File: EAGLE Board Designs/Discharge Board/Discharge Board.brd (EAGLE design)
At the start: 57.1 x 77.1 mm, 21 parts, among them J100 CONNECTOR-2_MICROFIT_SMD_RIGH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, J101 CONNECTOR-2_MICROFIT_SMD_RIGH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, K1 RELAY_SPST_NC_POLARIZED_D_24

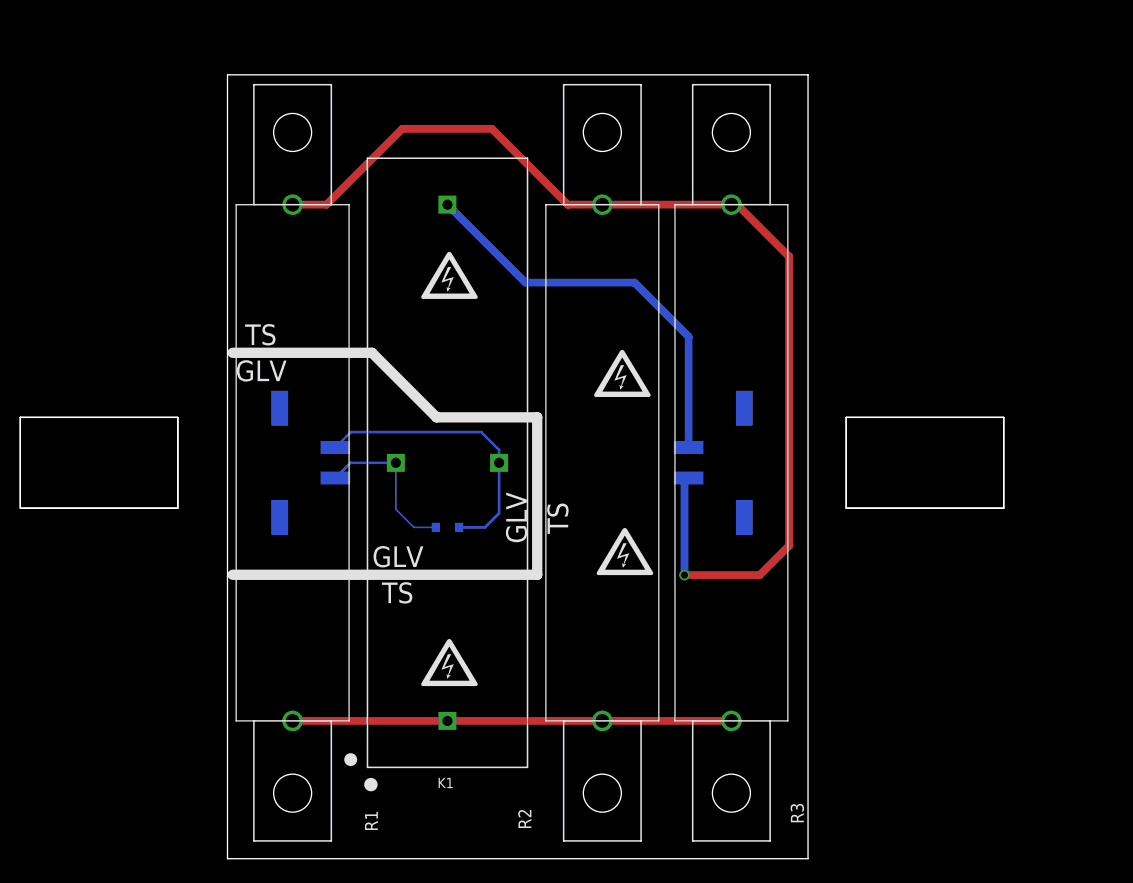
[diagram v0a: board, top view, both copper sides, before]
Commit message: Replace B20 with B20-SHORTENED
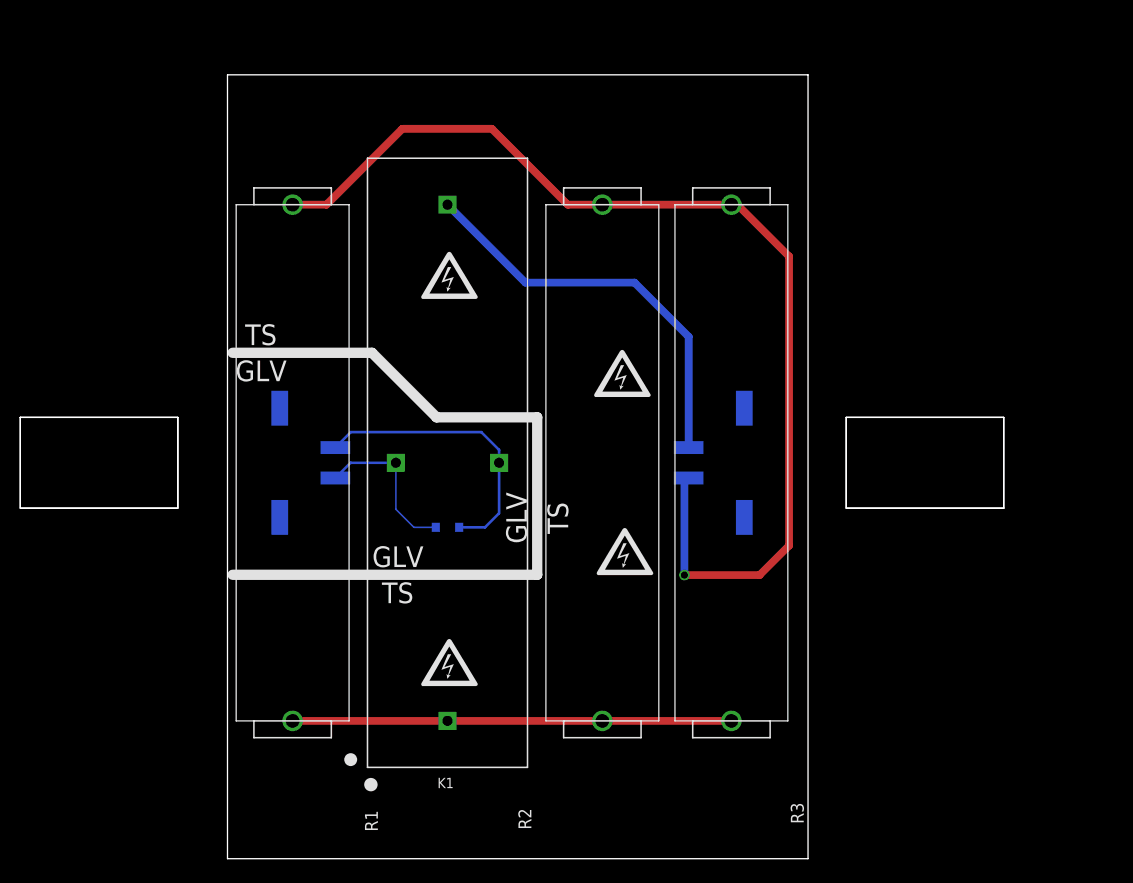
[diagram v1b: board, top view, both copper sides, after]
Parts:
- R1, R2, R3: value RESISTOR_B20_15K -> RESISTOR_B20-SHORTENED_15K; device HyTechDevices:B20 -> HyTechDevices:B20-SHORTENED
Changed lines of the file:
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@@
 <attribute name="NAME" x="21.464" y="7.96" size="1.016" layer="21" font="vector" rot="R180" align="bottom-center"/>
 </element>
-<element name="R1" library="HyTechDevices" package="B20" value="RESISTOR_B20_15K" x="6.41" y="38.96" smashed="yes" rot="R90">
+<element name="R1" library="HyTechDevices" package="B20-SHORTENED" value="RESISTOR_B20-SHORTENED_15K" x="6.41" y="38.96" smashed="yes" rot="R90">
 <attribute name="DKPN" value="B20J15KE-ND" x="66.1" y="89.76" size="1.778" layer="27" rot="R90" display="off"/>
 <attribute name="MANUFACTURER" value="Ohmite" x="66.1" y="89.76" size="1.778" layer="27" rot="R90" display="off"/>
@@
 <attribute name="VOLTAGE_MAX" value="750V" x="66.1" y="89.76" size="1.778" layer="27" rot="R90" display="off"/>
 </element>
-<element name="R2" library="HyTechDevices" package="B20" value="RESISTOR_B20_15K" x="36.89" y="38.96" smashed="yes" rot="R90">
+<element name="R2" library="HyTechDevices" package="B20-SHORTENED" value="RESISTOR_B20-SHORTENED_15K" x="36.89" y="38.96" smashed="yes" rot="R90">
 <attribute name="DKPN" value="B20J15KE-ND" x="111.82" y="89.76" size="1.778" layer="27" rot="R90" display="off"/>
 <attribute name="MANUFACTURER" value="Ohmite" x="111.82" y="89.76" size="1.778" layer="27" rot="R90" display="off"/>
@@
 <attribute name="VOLTAGE_MAX" value="750V" x="111.82" y="89.76" size="1.778" layer="27" rot="R90" display="off"/>
 </element>
-<element name="R3" library="HyTechDevices" package="B20" value="RESISTOR_B20_15K" x="49.59" y="38.96" smashed="yes" rot="R90">
+<element name="R3" library="HyTechDevices" package="B20-SHORTENED" value="RESISTOR_B20-SHORTENED_15K" x="49.59" y="38.96" smashed="yes" rot="R90">
 <attribute name="DKPN" value="B20J15KE-ND" x="139.76" y="89.76" size="1.778" layer="27" rot="R90" display="off"/>
 <attribute name="MANUFACTURER" value="Ohmite" x="139.76" y="89.76" size="1.778" layer="27" rot="R90" display="off"/>

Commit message: adjusted labels
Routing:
- net N$5: track 106.8 -> 104.3 mm
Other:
- board size 57.1 x 77.1 mm -> 57.1 x 69.5 mm
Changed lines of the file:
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@@
 <setting verticaltext="up"/>
 </settings>
-<grid distance="10" unitdist="mil" unit="mil" style="lines" multiple="1" display="no" altdistance="5" altunitdist="mil" altunit="mil"/>
+<grid distance="1" unitdist="mil" unit="mil" style="lines" multiple="1" display="no" altdistance="5" altunitdist="mil" altunit="mil"/>
 <layers>
 <layer number="1" name="Top" color="4" fill="1" visible="yes" active="yes"/>
@@
 <plain>
 <wire x1="0" y1="0" x2="57.13" y2="0" width="0" layer="20"/>
-<wire x1="57.13" y1="0" x2="57.13" y2="77.14" width="0" layer="20"/>
-<wire x1="57.13" y1="77.14" x2="0" y2="77.14" width="0" layer="20"/>
-<wire x1="0" y1="77.14" x2="0" y2="0" width="0" layer="20"/>
+<wire x1="57.13" y1="0" x2="57.13" y2="69.52" width="0" layer="20"/>
+<wire x1="57.13" y1="69.52" x2="0" y2="69.52" width="0" layer="20"/>
+<wire x1="0" y1="69.52" x2="0" y2="0" width="0" layer="20"/>
 <dimension x1="59" y1="77" x2="59" y2="1" x3="70" y3="39" textsize="1.778" layer="1" dtype="diameter"/>
 <dimension x1="1" y1="79" x2="57" y2="79" x3="29" y3="80.317" textsize="1.778" layer="1" dtype="diameter"/>
@@
 <attribute name="MOPN" value="588-B20J15KE" x="66.1" y="89.76" size="1.778" layer="27" rot="R90" display="off"/>
 <attribute name="MPN" value="B20J15KE" x="66.1" y="89.76" size="1.778" layer="27" rot="R90" display="off"/>
-<attribute name="NAME" x="13.529" y="3.712" size="1.27" layer="21" font="vector" rot="R270" align="bottom-center"/>
+<attribute name="NAME" x="6.4806" y="10.4994" size="1.27" layer="21" font="vector" rot="R180" align="bottom-center"/>
 <attribute name="POWER" value="20W" x="66.1" y="89.76" size="1.778" layer="27" rot="R90" display="off"/>
 <attribute name="RESISTANCE" value="15K" x="66.1" y="89.76" size="1.778" layer="27" rot="R90" display="off"/>
@@
 <attribute name="MOPN" value="588-B20J15KE" x="111.82" y="89.76" size="1.778" layer="27" rot="R90" display="off"/>
 <attribute name="MPN" value="B20J15KE" x="111.82" y="89.76" size="1.778" layer="27" rot="R90" display="off"/>
-<attribute name="NAME" x="29.905" y="3.908" size="1.27" layer="21" font="vector" rot="R90" align="bottom-center"/>
+<attribute name="NAME" x="36.732" y="10.4994" size="1.27" layer="21" font="vector" rot="R180" align="bottom-center"/>
 <attribute name="POWER" value="20W" x="111.82" y="89.76" size="1.778" layer="27" rot="R90" display="off"/>
 <attribute name="RESISTANCE" value="15K" x="111.82" y="89.76" size="1.778" layer="27" rot="R90" display="off"/>
@@
 <attribute name="MOPN" value="588-B20J15KE" x="139.76" y="89.76" size="1.778" layer="27" rot="R90" display="off"/>
 <attribute name="MPN" value="B20J15KE" x="139.76" y="89.76" size="1.778" layer="27" rot="R90" display="off"/>
-<attribute name="NAME" x="55.439" y="4.474" size="1.27" layer="21" font="vector" rot="R270" align="bottom-center"/>
+<attribute name="NAME" x="49.5844" y="10.4994" size="1.27" layer="21" font="vector" rot="R180" align="bottom-center"/>
 <attribute name="POWER" value="20W" x="139.76" y="89.76" size="1.778" layer="27" rot="R90" display="off"/>
 <attribute name="RESISTANCE" value="15K" x="139.76" y="89.76" size="1.778" layer="27" rot="R90" display="off"/>
@@
 <wire x1="49.59" y1="64.36" x2="36.89" y2="64.36" width="0.762" layer="1"/>
 <wire x1="36.89" y1="64.36" x2="33.4864" y2="64.36" width="0.762" layer="1"/>
-<wire x1="33.4864" y1="64.36" x2="26.0188" y2="71.8276" width="0.762" layer="1"/>
-<wire x1="26.0188" y1="71.8276" x2="17.205" y2="71.8276" width="0.762" layer="1"/>
-<wire x1="17.205" y1="71.8276" x2="9.7374" y2="64.36" width="0.762" layer="1"/>
+<wire x1="33.4864" y1="64.36" x2="29.0668" y2="68.7796" width="0.762" layer="1"/>
+<wire x1="29.0668" y1="68.7796" x2="14.157" y2="68.7796" width="0.762" layer="1"/>
+<wire x1="14.157" y1="68.7796" x2="9.7374" y2="64.36" width="0.762" layer="1"/>
 <wire x1="9.7374" y1="64.36" x2="6.41" y2="64.36" width="0.762" layer="1"/>
 <wire x1="55.2636" y1="59.2706" x2="50.1742" y2="64.36" width="0.762" layer="1"/>

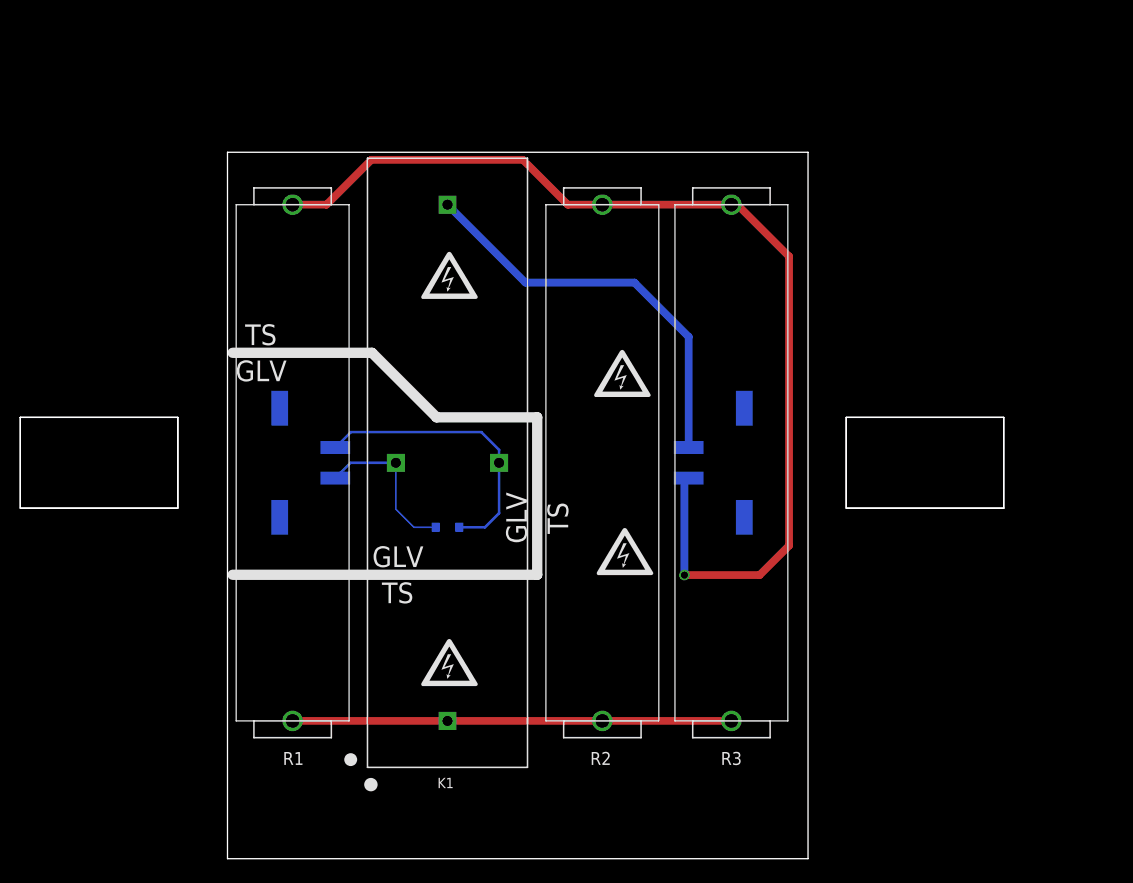
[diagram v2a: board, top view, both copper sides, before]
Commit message: Update Discharge Board.brd
Adjusted board size
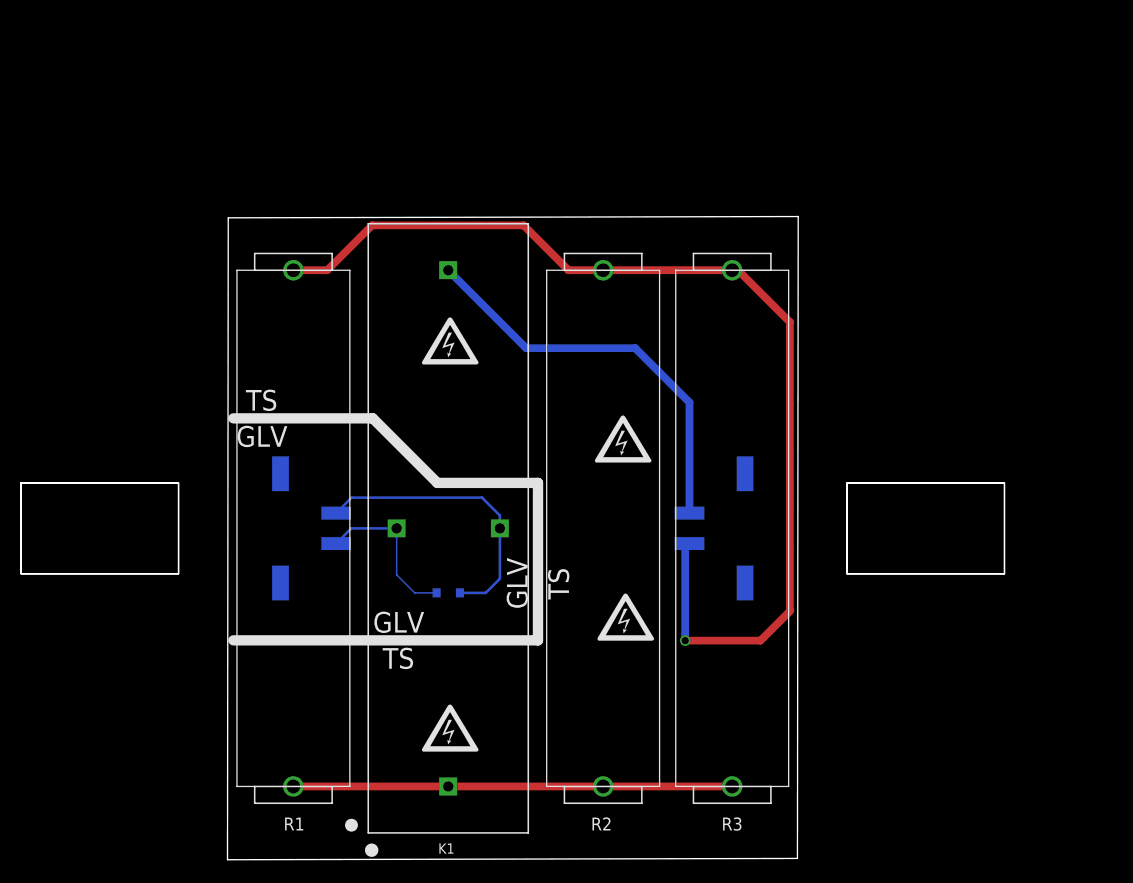
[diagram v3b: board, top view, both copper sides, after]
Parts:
- moved U$10 6.45 mm to (21.9, 51.0)
- moved U$11 6.45 mm to (21.9, 51.0)
- moved D100 6.45 mm to (21.7, 26.2)
- moved J100 6.45 mm to (50.9, 32.5)
- moved J101 6.45 mm to (5.22, 32.5)
- moved K1 6.45 mm to (21.7, 32.5)
- moved R1 6.45 mm to (6.49, 32.5)
- moved R2 6.45 mm to (37.0, 32.5)
- moved R3 6.45 mm to (49.7, 32.5)
- moved U$1 6.45 mm to (3.38, 41.6)
- moved U$12 6.45 mm to (38.9, 41.3)
- moved U$13 6.45 mm to (39.2, 23.8)
- moved U$14 6.45 mm to (21.9, 12.9)
- moved U$2 6.45 mm to (16.8, 23.3)
- moved U$3 6.45 mm to (3.38, 45.1)
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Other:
- board size 57.1 x 69.5 mm -> 56.2 x 63.3 mm

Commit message: Added 4 m3 mounting holes at correct distances away
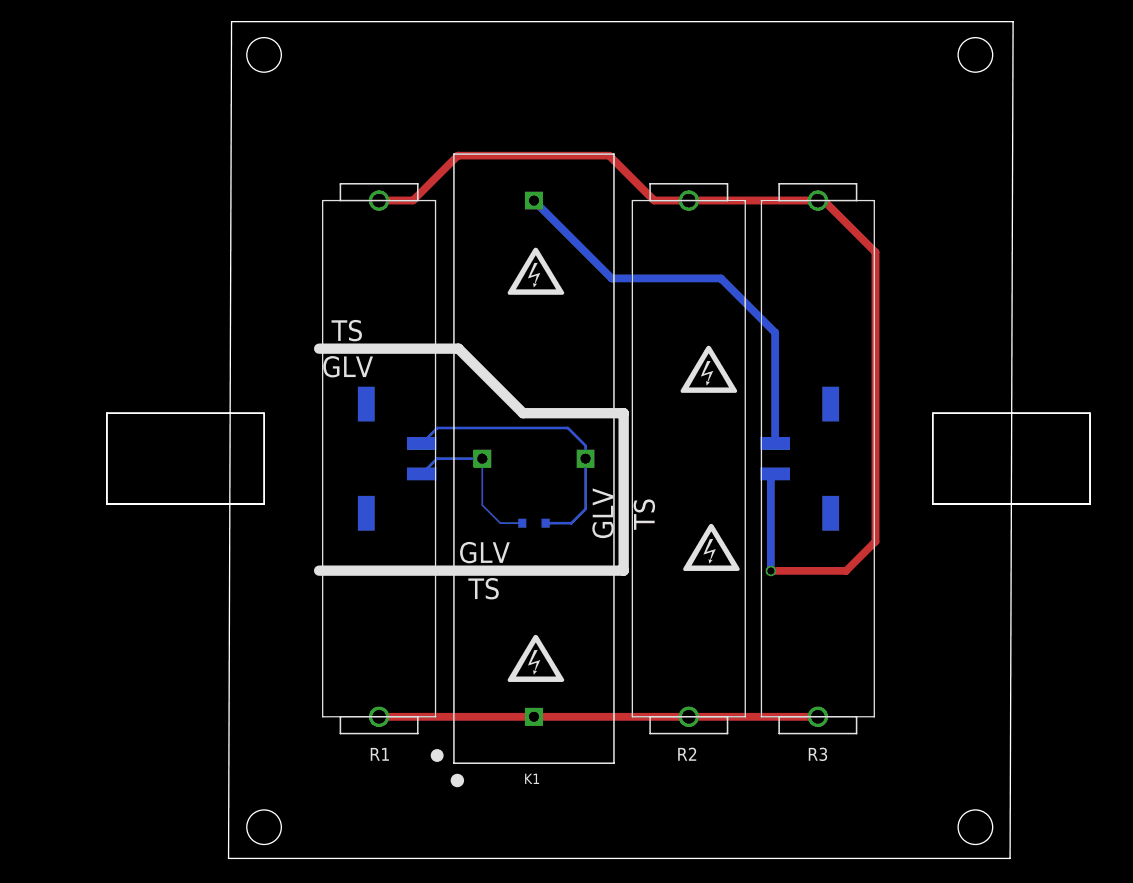
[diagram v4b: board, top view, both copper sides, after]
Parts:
- added U$15, U$16, U$17, U$18: (no value), HyTechManufacturing:MOUNTING_M3
- moved U$10 10.9 mm to (30.4, 57.8)
- moved U$11 10.9 mm to (30.4, 57.8)
- moved U$3 10.9 mm to (11.8, 52.0)
- moved U$13 10.9 mm to (47.6, 30.6)
- moved U$14 10.9 mm to (30.4, 19.7)
- moved U$2 10.9 mm to (25.3, 30.1)
- moved U$4 10.9 mm to (25.3, 26.6)
- moved U$7 10.9 mm to (30.4, 19.7)
- moved U$9 10.9 mm to (47.6, 30.6)
- moved D100 10.9 mm to (30.2, 33.0)
- moved J100 10.9 mm to (59.4, 39.4)
- moved J101 10.9 mm to (13.6, 39.4)
- moved K1 10.9 mm to (30.2, 39.4)
- moved R1 10.9 mm to (14.9, 39.4)
- moved R2 10.9 mm to (45.4, 39.4)
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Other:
- board size 56.2 x 63.3 mm -> 77.2 x 82.3 mm

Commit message: adjusted dimensions to 70mm x 56mm
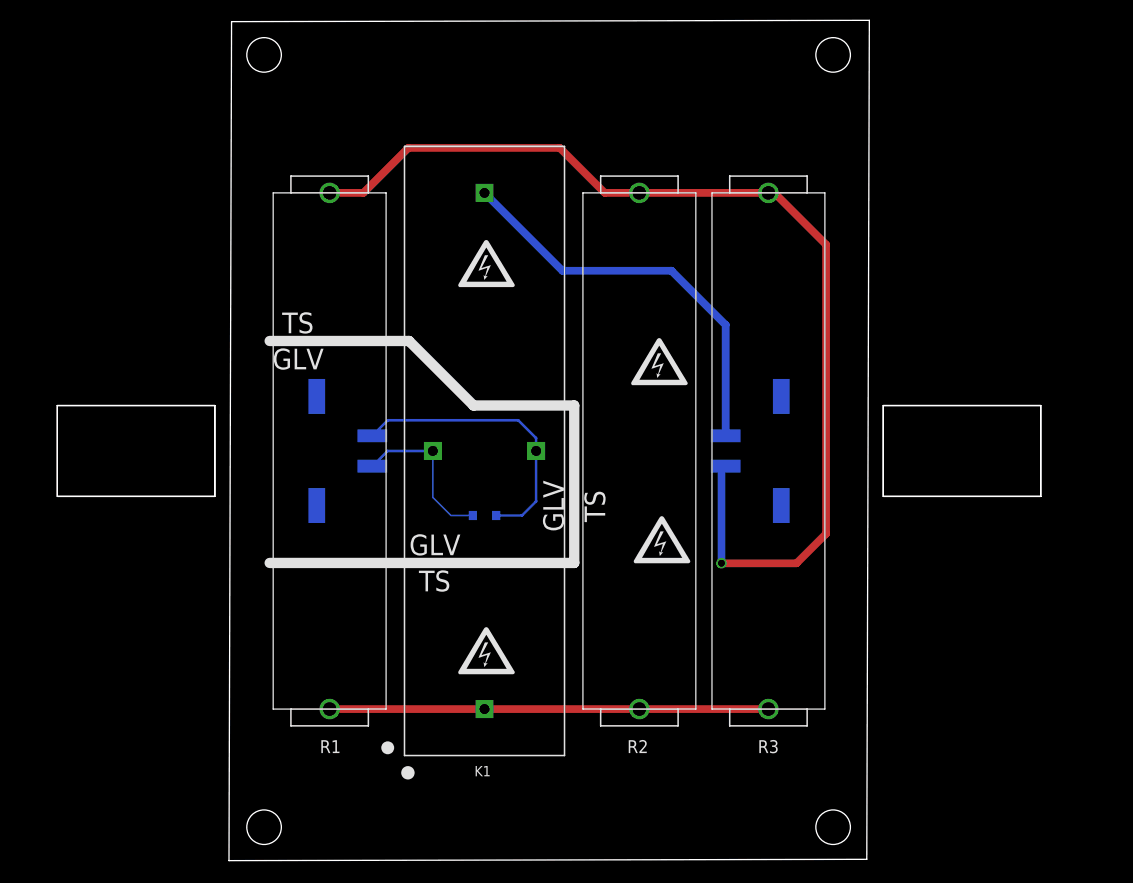
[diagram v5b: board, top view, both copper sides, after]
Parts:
- moved U$16 14.0 mm to (59.6, 3.10)
- moved U$18 14.0 mm to (59.6, 79.1)
- moved U$14 4.92 mm to (25.5, 20.5)
- moved U$7 4.92 mm to (25.5, 20.5)
- moved U$10 4.92 mm to (25.5, 58.6)
- moved U$11 4.92 mm to (25.5, 58.6)
- moved D100 4.92 mm to (25.3, 33.8)
- moved J100 4.92 mm to (54.5, 40.1)
- moved J101 4.92 mm to (8.78, 40.1)
- moved K1 4.92 mm to (25.3, 40.1)
- moved R1 4.92 mm to (10.1, 40.1)
- moved R2 4.92 mm to (40.5, 40.1)
- moved R3 4.92 mm to (53.2, 40.1)
- moved U$1 4.92 mm to (6.95, 49.2)
- moved U$12 4.92 mm to (42.5, 48.9)
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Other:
- board size 77.2 x 82.3 mm -> 63 x 82.7 mm

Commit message: slight adjustments
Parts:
- moved U$17 6.00 mm to (3.60, 73.1)
- moved U$18 6.00 mm to (59.6, 73.1)
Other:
- board size 63 x 82.7 mm -> 62.8 x 76.9 mm
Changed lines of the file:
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@@
 <plain>
 <wire x1="0.1478" y1="-0.1898" x2="62.9122" y2="-0.0602" width="0" layer="20"/>
-<wire x1="62.9122" y1="-0.0602" x2="63.165" y2="82.5038" width="0" layer="20"/>
-<wire x1="63.165" y1="82.5038" x2="0.4006" y2="82.3742" width="0" layer="20"/>
-<wire x1="0.4006" y1="82.3742" x2="0.1478" y2="-0.1898" width="0" layer="20"/>
+<wire x1="62.9122" y1="-0.0602" x2="62.948" y2="76.7418" width="0" layer="20"/>
+<wire x1="62.948" y1="76.7418" x2="0.1836" y2="76.6122" width="0" layer="20"/>
+<wire x1="0.1836" y1="76.6122" x2="0.1478" y2="-0.1898" width="0" layer="20"/>
 <circle x="17.756" y="8.4542" radius="0.3302" width="0.6604" layer="21"/>
 <wire x1="17.867" y1="50.9484" x2="24.217" y2="44.5984" width="1.016" layer="21"/>
@@
 <element name="U$15" library="HyTechManufacturing" package="MOUNTING_M3" value="" x="3.6" y="3.1" smashed="yes"/>
 <element name="U$16" library="HyTechManufacturing" package="MOUNTING_M3" value="" x="59.6" y="3.1" smashed="yes"/>
-<element name="U$17" library="HyTechManufacturing" package="MOUNTING_M3" value="" x="3.6" y="79.1" smashed="yes"/>
-<element name="U$18" library="HyTechManufacturing" package="MOUNTING_M3" value="" x="59.6" y="79.1" smashed="yes"/>
+<element name="U$17" library="HyTechManufacturing" package="MOUNTING_M3" value="" x="3.6" y="73.1" smashed="yes"/>
+<element name="U$18" library="HyTechManufacturing" package="MOUNTING_M3" value="" x="59.6" y="73.1" smashed="yes"/>
 </elements>
 <signals>
